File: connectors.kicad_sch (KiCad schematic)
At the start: 33 parts, among them J10 Conn_01x06, J11 Conn_01x04, J12 USB_C_Receptacle_USB2.0_16P, J14 Conn_01x03, J6 FTSH-107-01-L-DV-K-TR, J7 Conn_01x03, J8 Conn_01x02, J9 Conn_01x07, Q7 AO3400A, Q8 AO3400A

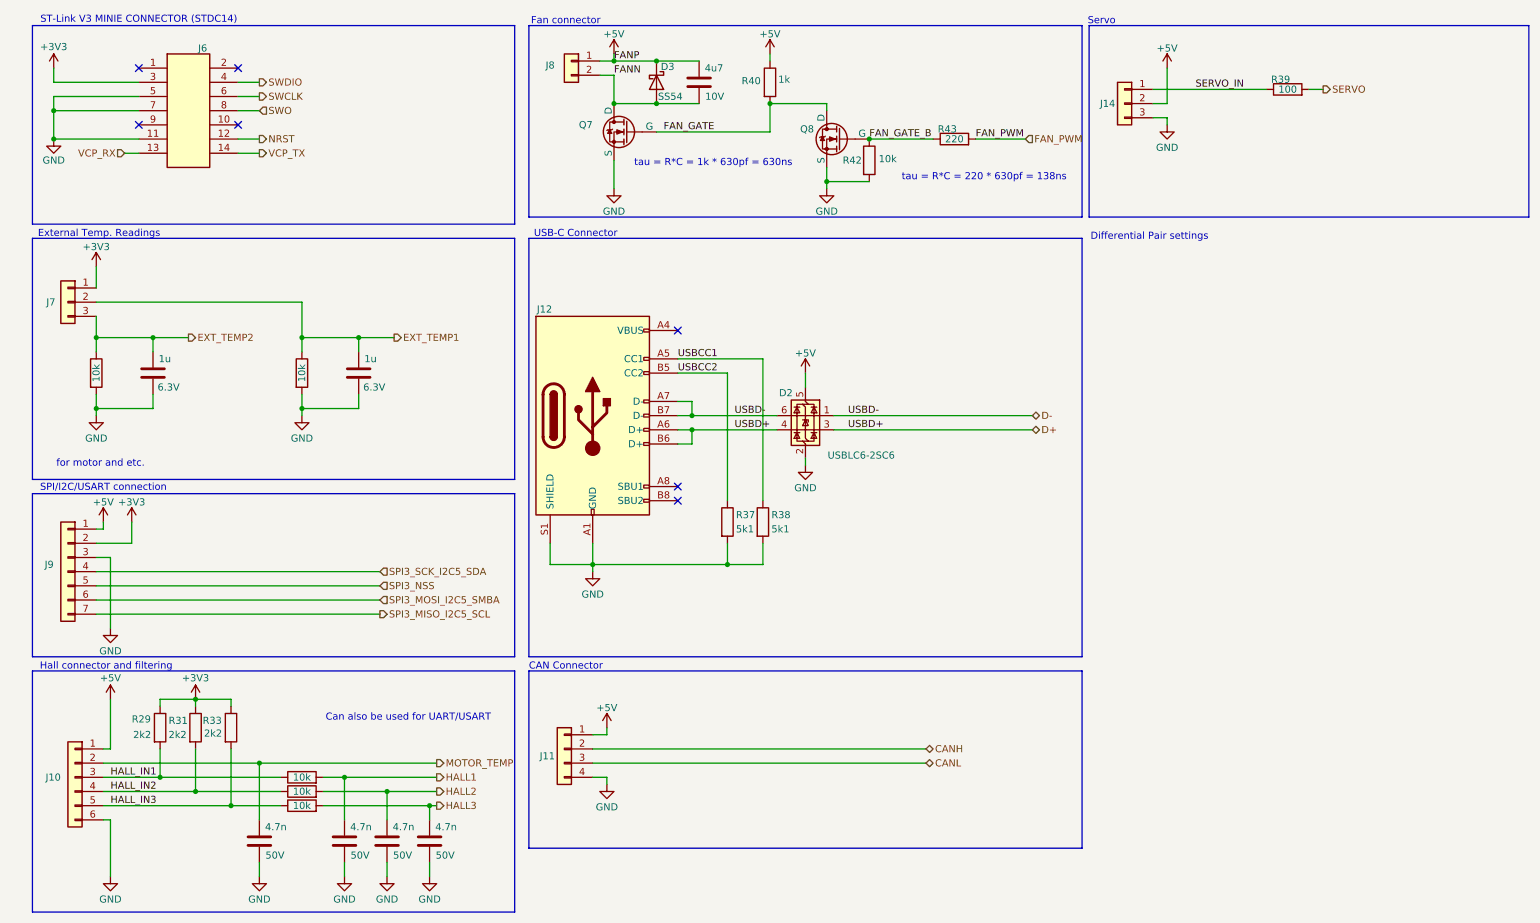
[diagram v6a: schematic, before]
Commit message: ERC errors have been fixed. XTAL changed to 12MHz. WiP DRC errors.
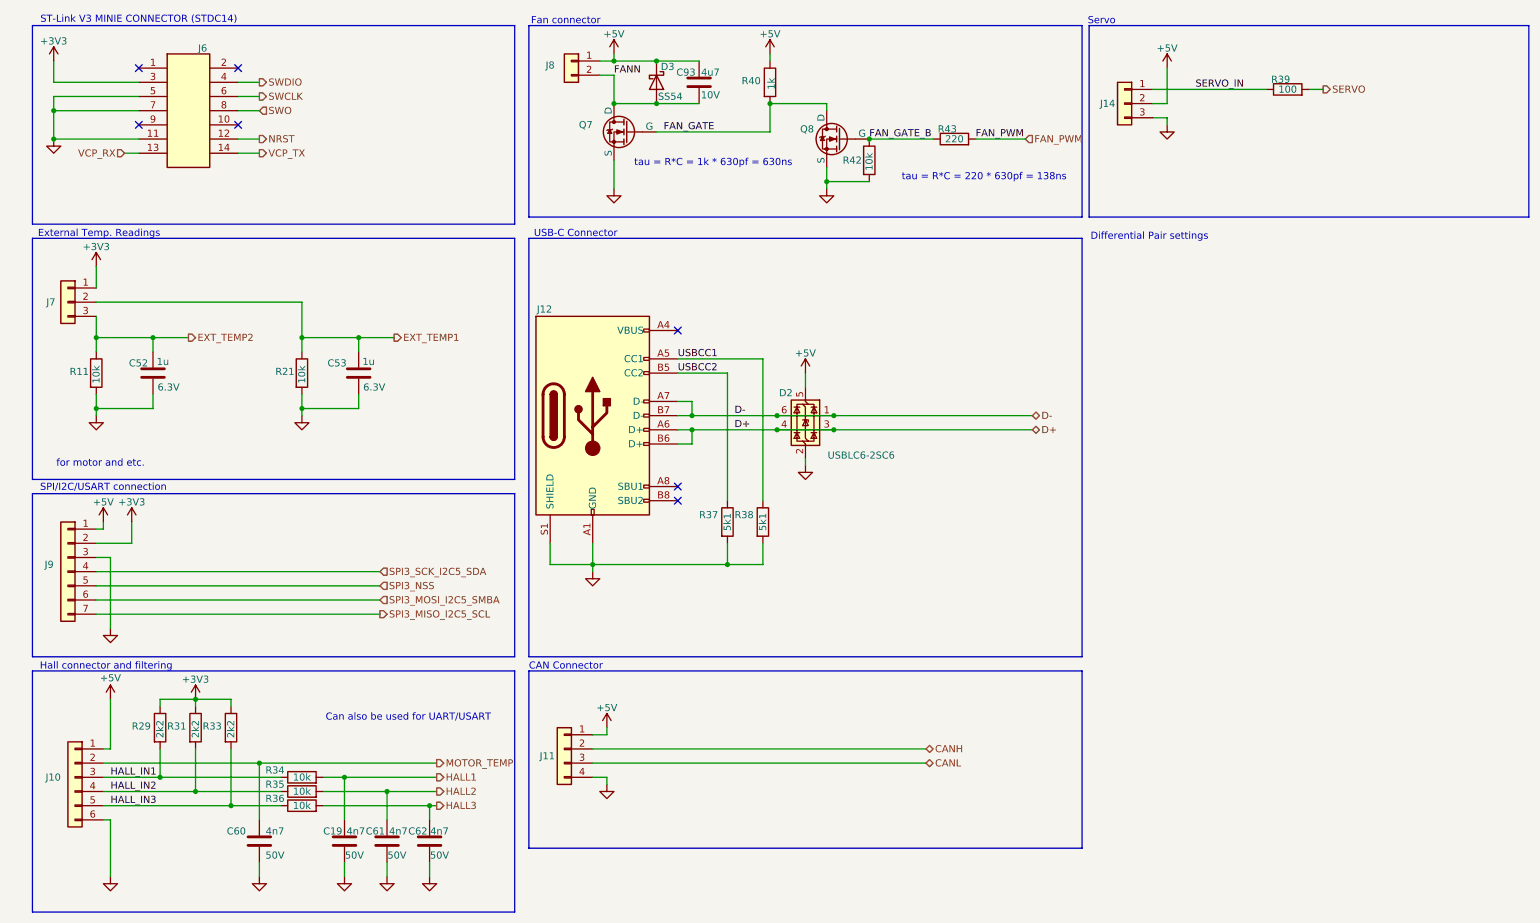
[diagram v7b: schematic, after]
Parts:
- removed R29, R31, R33: 2k2, Resistor_SMD:R_0402_1005Metric, symbol NanoGaN:R
- removed R40: 0402WGF1001TCE, Resistor_SMD:R_0402_1005Metric, symbol NanoGaN:R
- added R29, R31, R33, R40: 0402WGF1001TCE, Resistor_SMD:R_0402_1005Metric, symbol Device:R
- C19, C60, C61, C62: value 4.7n -> 0402B472K500NT; Capacitance (none) -> 4n7
- C52, C53: value 1u -> CL05B105KQ5NQNC; Capacitance (none) -> 1u
- C93: value 4u7 -> CL05A475MP5NRNC; Capacitance (none) -> 4u7
- R11, R21, R34, R35, R36: value 10k -> 0402WGF1002TCE; Resistance (none) -> 10k
- R37, R38: value 5k1 -> 0402WGF5101TCE; Resistance (none) -> 5k1
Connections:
- net +3V3: now also R29.1, R31.1, R33.1
- net +5V: now also R40.1
- net FAN_GATE: now also R40.2
- net HALL_IN1: now also R29.2
- net HALL_IN2: now also R31.2
- net HALL_IN3: now also R33.2
